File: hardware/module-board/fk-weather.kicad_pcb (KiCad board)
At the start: 2 copper layers, 37.5 x 103 mm, 72 parts, among them J1 MICRO-USB, J10 Conn_01x06, J11 Conn_01x06, J2 Conn_01x05, J3 CONN_01x03_SERIAL, J4 Conn_01x04, J5 Conn_01x02, J6 CONN_02x05_SWD, J7 Conn_01x05, Q4 2N7002LT1G, SW1 SPNO, U1 ATSAMD21G18A-AU, U2 MCP1700T-XXX2E, U3 TPS2051B, U4 S25FL1xxK0XM, U5 SK6812, U6 PCF8523, Y1 FC-135, Y2 FC-135

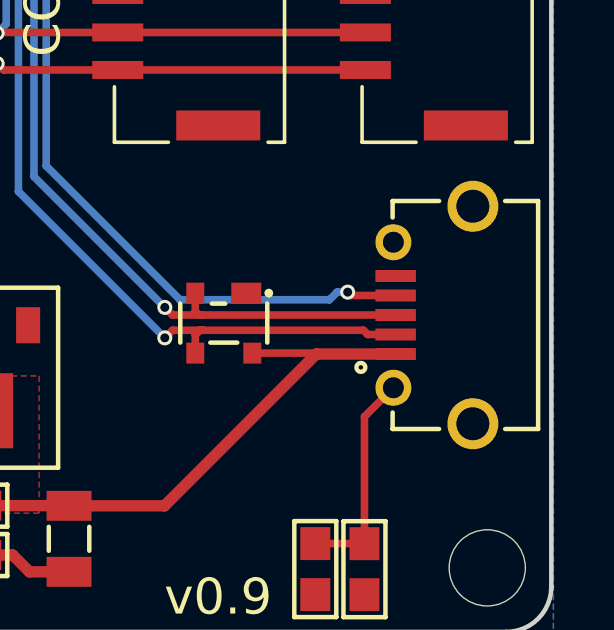
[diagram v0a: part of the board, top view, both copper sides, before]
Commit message: New USB for vertical entry.
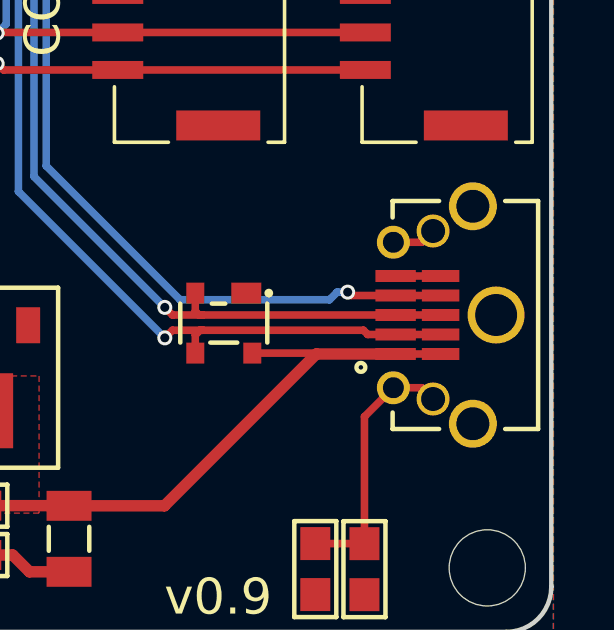
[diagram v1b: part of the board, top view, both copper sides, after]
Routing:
- net VUSB: track 23.9 -> 25.4 mm
- net Net-(J1-Pad4): track 41.1 -> 42.6 mm
- net GND: track 39.7 -> 41.2 mm
- net /USB-: track 36.6 -> 38.1 mm
- net /USB+: track 35.7 -> 37.2 mm
- net Net-(J1-Pad7): track 0.00 -> 1.48 mm
- net Net-(C10-Pad1): track 7.24 -> 8.72 mm
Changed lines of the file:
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@@
     (thickness 1.6)
     (drawings 16)
-    (tracks 696)
+    (tracks 705)
     (zones 0)
     (modules 72)
@@
     (visible_elements 7FFFDF7F)
     (pcbplotparams
-      (layerselection 0x010fc_80000001)
+      (layerselection 0x010fc_ffffffff)
       (usegerberextensions false)
       (usegerberattributes false)
@@
     (uvia_drill 0.1)
   )
+  (module conservify:MICRO-USB (layer F.Cu)
+    (at 118.364 189.738 90)
+    (tags MICRO-USB)
+    (fp_text reference J1 (at -26.162 0 90) (layer F.SilkS) hide
+      (effects (font (size 0.8 0.8) (thickness 0.15)))
+    )
+    (fp_text value MICRO-USB (at 0 4.318 90) (layer F.Fab) hide
+      (effects (font (size 0.8 0.8) (thickness 0.15)))
+    )
+    (fp_line (start -3.8 3.3) (end 3.8 3.3) (layer F.SilkS) (width 0.15))
+    (fp_line (start -3.8 3.3) (end -3.8 2.2) (layer F.SilkS) (width 0.15))
+    (fp_line (start 3.8 2.2) (end 3.8 3.3) (layer F.SilkS) (width 0.15))
+    (fp_line (start -3.8 -1.55) (end -3.25 -1.55) (layer F.SilkS) (width 0.15))
+    (fp_line (start -3.8 0) (end -3.8 -1.55) (layer F.SilkS) (width 0.15))
+    (fp_line (start 3.8 -1.55) (end 3.25 -1.55) (layer F.SilkS) (width 0.15))
+    (fp_line (start 3.8 0) (end 3.8 -1.55) (layer F.SilkS) (width 0.15))
+    (fp_circle (center -1.746 -2.608) (end -1.796 -2.658) (layer F.SilkS) (width 0.3))
+    (fp_line (start 4.55 -2.4) (end -4.55 -2.4) (layer F.CrtYd) (width 0.05))
+    (fp_line (start 4.55 3.45) (end 4.55 -2.4) (layer F.CrtYd) (width 0.05))
+    (fp_line (start -4.55 3.45) (end 4.55 3.45) (layer F.CrtYd) (width 0.05))
+    (fp_line (start -4.55 -2.4) (end -4.55 3.45) (layer F.CrtYd) (width 0.05))
+    (pad 10 thru_hole circle (at 0 1.9 90) (size 1.9 1.9) (drill oval 1.4) (layers *.Cu *.Mask F.Paste))
+    (pad 9 thru_hole circle (at 3.625 1.125 90) (size 1.6 1.6) (drill oval 1.1) (layers *.Cu *.Mask F.Paste)
+      (net 40 "Net-(J1-Pad9)"))
+    (pad 8 thru_hole circle (at -3.625 1.125 90) (size 1.6 1.6) (drill oval 1.1) (layers *.Cu *.Mask F.Paste)
+      (net 39 "Net-(J1-Pad8)"))
+    (pad 7 thru_hole circle (at 2.425 -1.525 90) (size 1.1 1.1) (drill 0.7) (layers *.Cu *.Mask F.Paste)
+      (net 38 "Net-(J1-Pad7)"))
+    (pad 6 thru_hole circle (at -2.425 -1.525 90) (size 1.1 1.1) (drill 0.7) (layers *.Cu *.Mask F.Paste)
+      (net 35 "Net-(C10-Pad1)"))
+    (pad 5 smd rect (at 1.3 -1.45 90) (size 0.4 1.35) (layers F.Cu F.Paste F.Mask)
+      (net 1 GND))
+    (pad 4 smd rect (at 0.65 -1.45 90) (size 0.4 1.35) (layers F.Cu F.Paste F.Mask)
+      (net 37 "Net-(J1-Pad4)"))
+    (pad 3 smd rect (at 0 -1.45 90) (size 0.4 1.35) (layers F.Cu F.Paste F.Mask)
+      (net 27 /USB+))
+    (pad 2 smd rect (at -0.65 -1.45 90) (size 0.4 1.35) (layers F.Cu F.Paste F.Mask)
+      (net 26 /USB-))
+    (pad 1 smd rect (at -1.3 -1.45 90) (size 0.4 1.35) (layers F.Cu F.Paste F.Mask)
+      (net 36 VUSB))
+    (pad 6 thru_hole circle (at -2.8 -0.2 90) (size 1.1 1.1) (drill 0.8) (layers *.Cu *.Mask F.Paste)
+      (net 35 "Net-(C10-Pad1)"))
+    (pad 7 thru_hole circle (at 2.8 -0.2 90) (size 1.1 1.1) (drill 0.8) (layers *.Cu *.Mask F.Paste)
+      (net 38 "Net-(J1-Pad7)"))
+    (pad 5 smd rect (at 1.3 0.05 90) (size 0.4 1.25) (layers F.Cu F.Paste F.Mask)
+      (net 1 GND))
+    (pad 4 smd rect (at 0.65 0.05 90) (size 0.4 1.25) (layers F.Cu F.Paste F.Mask)
+      (net 37 "Net-(J1-Pad4)"))
+    (pad 3 smd rect (at 0 0.05 90) (size 0.4 1.25) (layers F.Cu F.Paste F.Mask)
+      (net 27 /USB+))
+    (pad 2 smd rect (at -0.65 0.05 90) (size 0.4 1.25) (layers F.Cu F.Paste F.Mask)
+      (net 26 /USB-))
+    (pad 1 smd rect (at -1.3 0.05 90) (size 0.4 1.25) (layers F.Cu F.Paste F.Mask)
+      (net 36 VUSB))
+  )
   (module conservify:conservify_text_negative_4000 (layer F.Cu)
     (at 88.519 112.522 270)
@@
       (xy -6.476371 -1.79874)) (layer F.SilkS) (width 0.01))
   )
-  (module conservify:MICRO-USB (layer F.Cu)
-    (at 118.364 189.738 90)
-    (tags MICRO-USB)
-    (fp_text reference J1 (at -26.162 0 90) (layer F.SilkS) hide
-      (effects (font (size 0.8 0.8) (thickness 0.15)))
-    )
-    (fp_text value MICRO-USB (at 0 4.318 90) (layer F.Fab) hide
-      (effects (font (size 0.8 0.8) (thickness 0.15)))
-    )
-    (fp_line (start -4.55 -2.4) (end -4.55 3.45) (layer F.CrtYd) (width 0.05))
-    (fp_line (start -4.55 3.45) (end 4.55 3.45) (layer F.CrtYd) (width 0.05))
-    (fp_line (start 4.55 3.45) (end 4.55 -2.4) (layer F.CrtYd) (width 0.05))
-    (fp_line (start 4.55 -2.4) (end -4.55 -2.4) (layer F.CrtYd) (width 0.05))
-    (fp_circle (center -1.746 -2.608) (end -1.796 -2.658) (layer F.SilkS) (width 0.3))
-    (fp_line (start 3.8 0) (end 3.8 -1.55) (layer F.SilkS) (width 0.15))
-    (fp_line (start 3.8 -1.55) (end 3.25 -1.55) (layer F.SilkS) (width 0.15))
-    (fp_line (start -3.8 0) (end -3.8 -1.55) (layer F.SilkS) (width 0.15))
-    (fp_line (start -3.8 -1.55) (end -3.25 -1.55) (layer F.SilkS) (width 0.15))
-    (fp_line (start 3.8 2.2) (end 3.8 3.3) (layer F.SilkS) (width 0.15))
-    (fp_line (start -3.8 3.3) (end -3.8 2.2) (layer F.SilkS) (width 0.15))
-    (fp_line (start -3.8 3.3) (end 3.8 3.3) (layer F.SilkS) (width 0.15))
-    (pad 1 smd rect (at -1.3 -1.45 90) (size 0.4 1.35) (layers F.Cu F.Paste F.Mask)
-      (net 36 VUSB))
-    (pad 2 smd rect (at -0.65 -1.45 90) (size 0.4 1.35) (layers F.Cu F.Paste F.Mask)
-      (net 26 /USB-))
-    (pad 3 smd rect (at 0 -1.45 90) (size 0.4 1.35) (layers F.Cu F.Paste F.Mask)
-      (net 27 /USB+))
-    (pad 4 smd rect (at 0.65 -1.45 90) (size 0.4 1.35) (layers F.Cu F.Paste F.Mask)
-      (net 37 "Net-(J1-Pad4)"))
-    (pad 5 smd rect (at 1.3 -1.45 90) (size 0.4 1.35) (layers F.Cu F.Paste F.Mask)
-      (net 1 GND))
-    (pad 6 thru_hole circle (at -2.425 -1.525 90) (size 1.2 1.2) (drill 0.7) (layers *.Cu *.Mask F.Paste)
-      (net 35 "Net-(C10-Pad1)"))
-    (pad 7 thru_hole circle (at 2.425 -1.525 90) (size 1.2 1.2) (drill 0.7) (layers *.Cu *.Mask F.Paste)
-      (net 38 "Net-(J1-Pad7)"))
-    (pad 8 thru_hole circle (at -3.625 1.125 90) (size 1.7 1.7) (drill oval 1.1) (layers *.Cu *.Mask F.Paste)
-      (net 39 "Net-(J1-Pad8)"))
-    (pad 9 thru_hole circle (at 3.625 1.125 90) (size 1.7 1.7) (drill oval 1.1) (layers *.Cu *.Mask F.Paste)
-      (net 40 "Net-(J1-Pad9)"))
-  )
   (module conservify:wurth_615006138421 (layer F.Cu)
     (at 115.923028 125.132668 270)
@@
   (segment (start 90.3249 149.4663) (end 90.3224 149.4638) (width 0.254) (layer F.Cu) (net 1))
   (segment (start 92.8269 149.4638) (end 92.8294 149.4663) (width 0.254) (layer F.Cu) (net 1))
+  (segment (start 116.914 188.438) (end 118.414 188.438) (width 0.254) (layer F.Cu) (net 1))
   (segment (start 98.789159 153.204241) (end 98.278693 153.204241) (width 0.254) (layer F.Cu) (net 2))
   (segment (start 98.278693 153.204241) (end 96.931517 154.551417) (width 0.254) (layer F.Cu) (net 2))
@@
   (via (at 103.8479 168.7703) (size 0.5) (drill 0.3) (layers F.Cu B.Cu) (net 26))
   (segment (start 102.537198 165.437831) (end 103.342461 166.243094) (width 0.254) (layer F.Cu) (net 26))
+  (segment (start 118.414 190.388) (end 116.914 190.388) (width 0.254) (layer F.Cu) (net 26))
   (segment (start 116.914 189.738) (end 110.49 189.738) (width 0.254) (layer F.Cu) (net 27))
   (segment (start 110.362 189.738) (end 110.49 189.738) (width 0.254) (layer F.Cu) (net 27))
@@
   (segment (start 102.890751 165.084278) (end 103.961587 166.155114) (width 0.254) (layer F.Cu) (net 27))
   (segment (start 103.961587 166.155114) (end 103.961587 167.444893) (width 0.254) (layer F.Cu) (net 27))
+  (segment (start 116.914 189.738) (end 118.414 189.738) (width 0.254) (layer F.Cu) (net 27))
   (segment (start 103.597858 162.114429) (end 104.3686 161.343687) (width 0.254) (layer F.Cu) (net 28))
   (segment (start 104.3686 161.343687) (end 104.3686 160.8074) (width 0.254) (layer F.Cu) (net 28))
@@
   (segment (start 115.8724 197.358) (end 115.8748 197.3604) (width 0.254) (layer F.Cu) (net 35))
   (segment (start 115.8724 197.108) (end 115.8748 197.1104) (width 0.254) (layer F.Cu) (net 35))
+  (segment (start 117.789 192.163) (end 118.164 192.538) (width 0.254) (layer F.Cu) (net 35))
+  (segment (start 116.839 192.163) (end 117.789 192.163) (width 0.254) (layer F.Cu) (net 35))
   (segment (start 103.163915 191.828661) (end 103.163915 190.728661) (width 0.381) (layer F.Cu) (net 36))
   (segment (start 103.219808 196.093462) (end 106.022508 196.093462) (width 0.381) (layer F.Cu) (net 36))
@@
   (segment (start 116.914 191.038) (end 116.439 191.038) (width 0.254) (layer F.Cu) (net 36))
   (segment (start 103.269808 196.093462) (end 103.219808 196.093462) (width 0.254) (layer F.Cu) (net 36))
+  (segment (start 116.914 191.038) (end 118.414 191.038) (width 0.254) (layer F.Cu) (net 36))
   (segment (start 108.546 161.6202) (end 108.546 163.2204) (width 0.254) (layer F.Cu) (net 37))
   (segment (start 109.855 163.195) (end 108.5714 163.195) (width 0.254) (layer F.Cu) (net 37))
@@
   (segment (start 115.428 189.088) (end 115.316 188.976) (width 0.254) (layer F.Cu) (net 37))
   (via (at 115.316 188.976) (size 0.5) (drill 0.3) (layers F.Cu B.Cu) (net 37))
+  (segment (start 118.414 189.088) (end 116.914 189.088) (width 0.254) (layer F.Cu) (net 37))
+  (segment (start 117.789 187.313) (end 118.164 186.938) (width 0.254) (layer F.Cu) (net 38))
+  (segment (start 116.839 187.313) (end 117.789 187.313) (width 0.254) (layer F.Cu) (net 38))
   (segment (start 106.027408 198.298362) (end 104.709253 198.298362) (width 0.381) (layer F.Cu) (net 41))
   (segment (start 104.709253 198.298362) (end 104.150808 197.739917) (width 0.381) (layer F.Cu) (net 41))

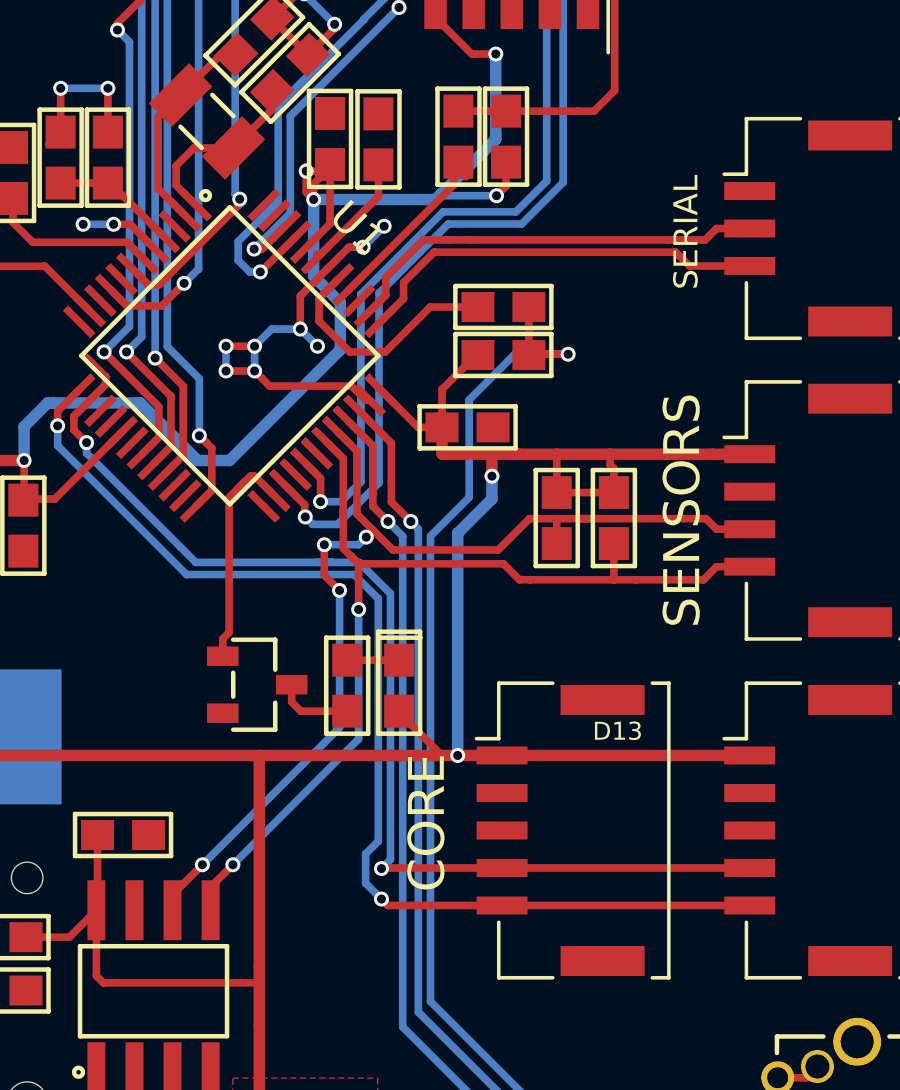
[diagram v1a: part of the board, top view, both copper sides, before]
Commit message: Fix a few small traces and the silkscreen.
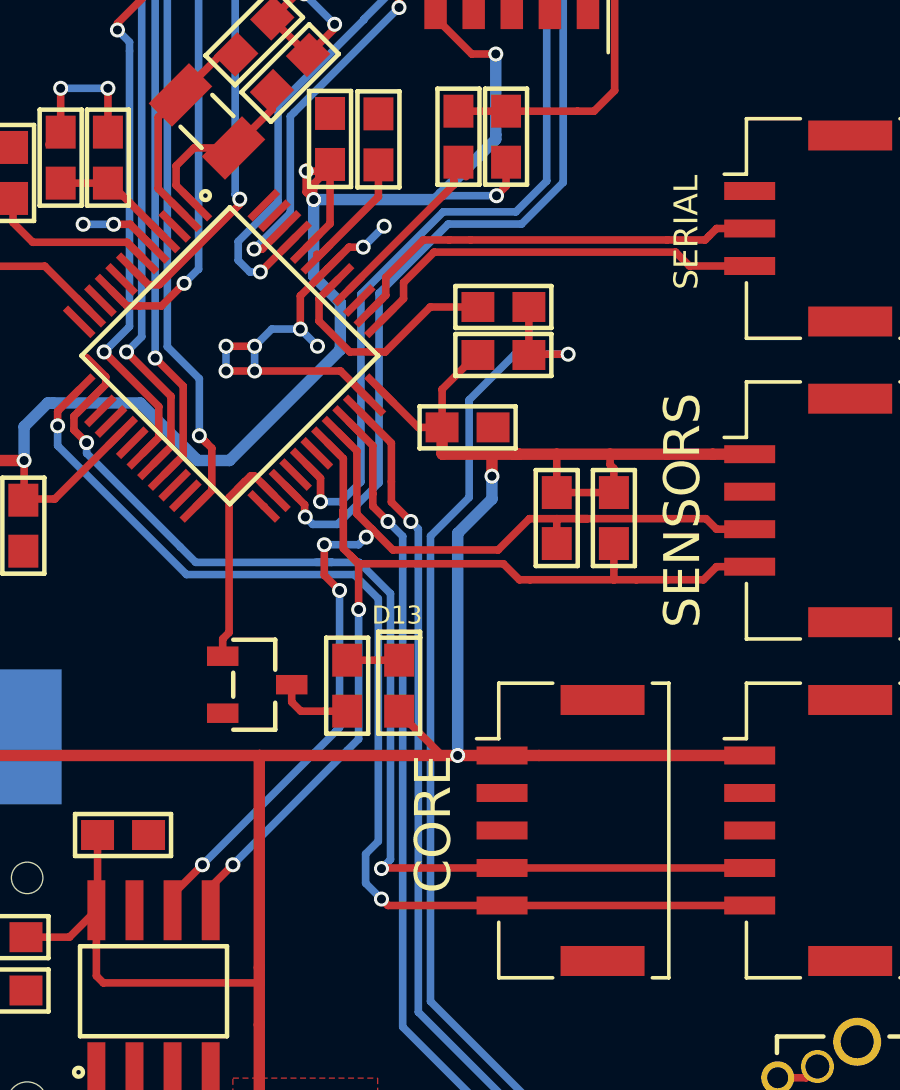
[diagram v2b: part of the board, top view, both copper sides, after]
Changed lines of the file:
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@@
     (thickness 1.6)
     (drawings 16)
-    (tracks 705)
+    (tracks 702)
     (zones 0)
     (modules 72)
@@
     (uvia_dia 0.3)
     (uvia_drill 0.1)
+  )
+  (module conservify:SJ_OPEN (layer F.Cu)
+    (at 88.138 148.59 90)
+    (descr "<b>Solder jumper</b>")
+    (fp_text reference J5 (at 0 -1.7 90) (layer F.SilkS) hide
+      (effects (font (size 0.8 0.8) (thickness 0.12)))
+    )
+    (fp_text value Conn_01x02 (at 0 1.6 90) (layer Eco1.User) hide
+      (effects (font (size 0.6 0.6) (thickness 0.1)))
+    )
+    (fp_line (start -1.397 -1.016) (end 1.397 -1.016) (layer F.SilkS) (width 0.1524))
+    (fp_line (start -1.651 0.762) (end -1.651 -0.762) (layer F.SilkS) (width 0.1524))
+    (fp_line (start 1.651 0.762) (end 1.651 -0.762) (layer F.SilkS) (width 0.1524))
+    (fp_arc (start 1.397 0.762) (end 1.397 1.016) (angle -90) (layer F.SilkS) (width 0.1524))
+    (fp_arc (start -1.397 0.762) (end -1.651 0.762) (angle -90) (layer F.SilkS) (width 0.1524))
+    (fp_arc (start -1.397 -0.762) (end -1.651 -0.762) (angle 90) (layer F.SilkS) (width 0.1524))
+    (fp_arc (start 1.397 -0.762) (end 1.397 -1.016) (angle 90) (layer F.SilkS) (width 0.1524))
+    (fp_line (start 1.397 1.016) (end -1.397 1.016) (layer F.SilkS) (width 0.1524))
+    (pad 2 smd rect (at 0.762 0 90) (size 1.1684 1.6002) (layers F.Cu F.Mask)
+      (net 71 /PERIPH_3V3))
+    (pad 1 smd rect (at -0.762 0 90) (size 1.1684 1.6002) (layers F.Cu F.Mask)
+      (net 4 3V3))
   )
   (module conservify:MICRO-USB (layer F.Cu)
@@
     )
   )
-  (module conservify:SJ_OPEN (layer F.Cu)
-    (at 88.138 148.59 90)
-    (descr "<b>Solder jumper</b>")
-    (fp_text reference J5 (at 0 -1.7 90) (layer F.SilkS) hide
-      (effects (font (size 0.8 0.8) (thickness 0.12)))
-    )
-    (fp_text value Conn_01x02 (at 0 1.6 90) (layer Eco1.User) hide
-      (effects (font (size 0.6 0.6) (thickness 0.1)))
-    )
-    (fp_line (start 1.397 1.016) (end -1.397 1.016) (layer F.SilkS) (width 0.1524))
-    (fp_arc (start 1.397 -0.762) (end 1.397 -1.016) (angle 90) (layer F.SilkS) (width 0.1524))
-    (fp_arc (start -1.397 -0.762) (end -1.651 -0.762) (angle 90) (layer F.SilkS) (width 0.1524))
-    (fp_arc (start -1.397 0.762) (end -1.651 0.762) (angle -90) (layer F.SilkS) (width 0.1524))
-    (fp_arc (start 1.397 0.762) (end 1.397 1.016) (angle -90) (layer F.SilkS) (width 0.1524))
-    (fp_line (start 1.651 0.762) (end 1.651 -0.762) (layer F.SilkS) (width 0.1524))
-    (fp_line (start -1.651 0.762) (end -1.651 -0.762) (layer F.SilkS) (width 0.1524))
-    (fp_line (start -1.397 -1.016) (end 1.397 -1.016) (layer F.SilkS) (width 0.1524))
-    (fp_line (start 1.016 0) (end 1.524 0) (layer Cmts.User) (width 0.1524))
-    (fp_line (start -1.016 0) (end -1.524 0) (layer Cmts.User) (width 0.1524))
-    (fp_arc (start -0.254 0) (end -0.254 0.127) (angle 180) (layer Cmts.User) (width 1.27))
-    (fp_arc (start 0.254 0) (end 0.254 -0.127) (angle 180) (layer Cmts.User) (width 1.27))
-    (pad 1 smd rect (at -0.762 0 90) (size 1.1684 1.6002) (layers F.Cu F.Mask)
-      (net 4 3V3))
-    (pad 2 smd rect (at 0.762 0 90) (size 1.1684 1.6002) (layers F.Cu F.Mask)
-      (net 71 /PERIPH_3V3))
-  )
   (module conservify:CAP-0603 (layer F.Cu)
     (at 99.3902 152.6032 225)
@@
     (tags "QFP 0.5")
     (attr smd)
-    (fp_text reference U1 (at 0 -6 315) (layer F.SilkS)
+    (fp_text reference U1 (at 0 -6 315) (layer F.SilkS) hide
       (effects (font (size 1 1) (thickness 0.15)))
     )
@@
     (effects (font (size 1.2 1.2) (thickness 0.2)))
   )
-  (gr_text CORE (at 105.156 178.816 90) (layer F.SilkS)
+  (gr_text CORE (at 105.3592 178.8541 90) (layer F.SilkS)
     (effects (font (size 1.2 1.2) (thickness 0.2)))
   )
@@
   (gr_line (start 86.103445 200.302083) (end 120.603445 200.302083) (layer Edge.Cuts) (width 0.15))
   (gr_line (start 120.603445 97.302083) (end 86.103445 97.302083) (layer Edge.Cuts) (width 0.15))
-  (gr_text D13 (at 111.506 175.768) (layer F.SilkS)
+  (gr_text D13 (at 104.1527 171.8945) (layer F.SilkS)
     (effects (font (size 0.6 0.6) (thickness 0.11)))
   )
@@
   (segment (start 101.0539 151.1808) (end 100.8126 151.1808) (width 0.254) (layer F.Cu) (net 1))
   (segment (start 100.8126 151.1808) (end 99.991241 152.002159) (width 0.254) (layer F.Cu) (net 1))
-  (segment (start 103.244305 164.730724) (end 103.109121 164.730724) (width 0.254) (layer F.Cu) (net 1))
-  (segment (start 99.652899 164.003799) (end 99.4029 163.7538) (width 0.254) (layer F.Cu) (net 1))
-  (segment (start 103.109121 164.730724) (end 102.635257 164.25686) (width 0.254) (layer F.Cu) (net 1))
-  (segment (start 99.90596 164.25686) (end 99.652899 164.003799) (width 0.254) (layer F.Cu) (net 1))
-  (segment (start 102.635257 164.25686) (end 99.90596 164.25686) (width 0.254) (layer F.Cu) (net 1))
   (segment (start 104.2289 112.4839) (end 105.064996 112.4839) (width 0.254) (layer F.Cu) (net 1))
   (segment (start 105.064996 112.4839) (end 105.370228 112.178668) (width 0.254) (layer F.Cu) (net 1))
@@
   (segment (start 92.8269 149.4638) (end 92.8294 149.4663) (width 0.254) (layer F.Cu) (net 1))
   (segment (start 116.914 188.438) (end 118.414 188.438) (width 0.254) (layer F.Cu) (net 1))
+  (segment (start 102.267381 163.7538) (end 103.244305 164.730724) (width 0.254) (layer F.Cu) (net 1))
+  (segment (start 99.4029 163.7538) (end 102.267381 163.7538) (width 0.254) (layer F.Cu) (net 1))
   (segment (start 98.789159 153.204241) (end 98.278693 153.204241) (width 0.254) (layer F.Cu) (net 2))
   (segment (start 98.278693 153.204241) (end 96.931517 154.551417) (width 0.254) (layer F.Cu) (net 2))
